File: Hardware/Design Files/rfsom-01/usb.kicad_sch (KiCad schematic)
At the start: 10 parts, among them U17 USB3320C-EZK, Y4 ECS-240-12-37B-CKY-TR

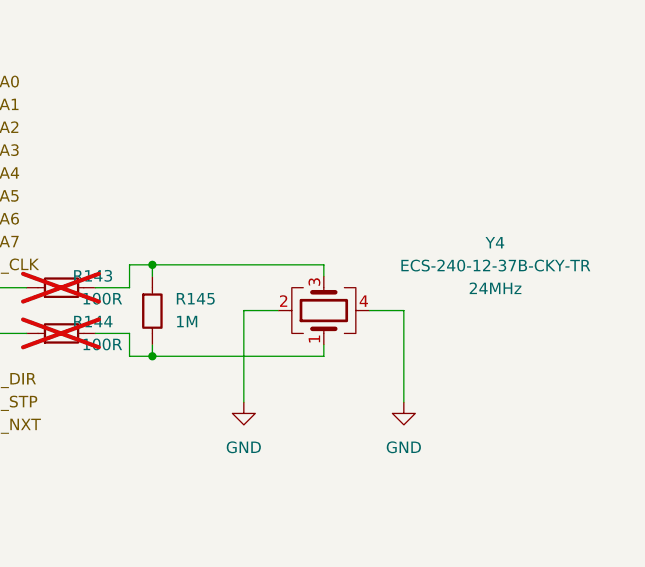
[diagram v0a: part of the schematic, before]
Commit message: routing changes; added mezzanine; added pl ram;
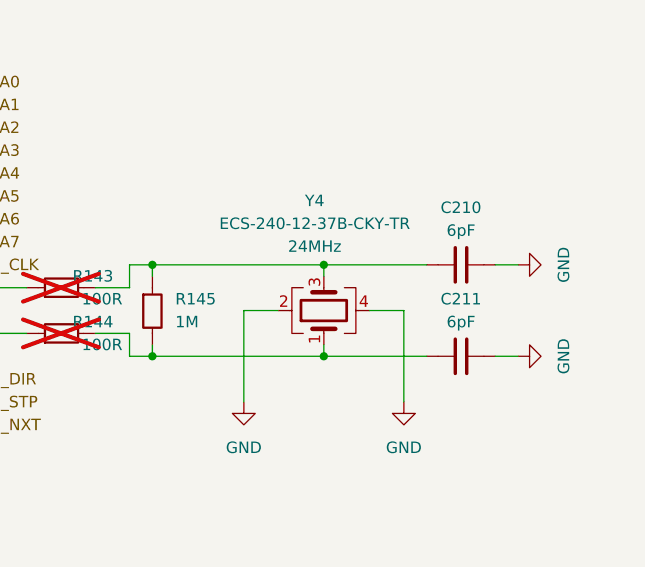
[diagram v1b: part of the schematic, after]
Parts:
- added C210, C211: CL10C060DB8NNNC, Capacitor_SMD:C_0603_1608Metric, symbol Capacitors:CL10C060DB8NNNC
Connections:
- net GND: now also C210.2, C211.2
- net at R143.2, R145.1, Y4.3: now also C210.1
- net at R144.2, R145.2, Y4.1: now also C211.1

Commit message: replaced pmic;
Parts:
- R141, R145: footprint Resistor_SMD:R_0603_1608Metric_Pad0.98x0.95mm_HandSolder -> Resistor_SMD:R_0603_1608Metric
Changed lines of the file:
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@@
 			)
 		)
-		(property "Footprint" "Resistor_SMD:R_0603_1608Metric_Pad0.98x0.95mm_HandSolder"
+		(property "Footprint" "Resistor_SMD:R_0603_1608Metric"
 			(at 217.17 73.66 0)
 			(effects
@@
 			)
 		)
-		(property "Footprint" "Resistor_SMD:R_0603_1608Metric_Pad0.98x0.95mm_HandSolder"
+		(property "Footprint" "Resistor_SMD:R_0603_1608Metric"
 			(at 130.81 96.52 0)
 			(effects
